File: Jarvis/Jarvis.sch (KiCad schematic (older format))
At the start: 139 parts, among them IC1 ADP1607, IC2 STM32F411CxUx, IC3 Si4460, IC4 MS5611-01BA03, IC5 MAX-8Q, IC6 MPU-9250, J1 PWR, J2 PYRO1, J3 ARM, J4 PYRO2, J5 PYRO3, J6 EXT, P1 SWD_TC, P2 SMA, Q1 NFET, Q2 NFET, Q3 NFET, Q4 NFET, Q5 PFET, Q6 PFET, Q7 PFET, U1 MICROSD, X1 434MHz ANT, X2 3mm LEDs, X3 ARM Switch, Y1 26MHz, Y2 30MHz

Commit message: Started PCB Layout
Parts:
- removed J2: PYRO1, agg:S02B-PASK-2, symbol CONN_01x02
- removed J4: PYRO2, agg:S02B-PASK-2, symbol CONN_01x02
- removed J5: PYRO3, agg:S02B-PASK-2, symbol CONN_01x02
- removed J6: EXT, symbol CONN_01x03
- removed Q4: NFET, symbol NFET
- removed Q6: PFET, symbol PFET
- removed R38, R39, R40: 10k, agg:0603-L, symbol R_Small
- added J2: PYRO, agg:S06B-PASK-2, symbol CONN_01x06
- added J4: EXT, agg:SIL-254P-04, symbol CONN_01x04
- added Q4: PFET, agg:SOT-23, symbol PFET
- added Q6: NFET, agg:SOT-23, symbol NFET
- added X4: Red LED, symbol PART
- D1, D2, D3: footprint (none) -> agg:0603-LED; Farnell (none) -> 1226372
- D4: footprint (none) -> agg:0603-LED; Farnell (none) -> 1226390
- IC5: footprint agg-unchecked:MAX-7Q -> Library:MAX-7Q
- IC6: footprint QFN-24-EP-MPU9250 -> agg:QFN-24-MPU9250
- J1: footprint (none) -> agg:S02B-PASK-2; Farnell 1702629 -> 1830747
- Q2, Q3: footprint (none) -> agg:SOT-23; Farnell (none) -> 1510761
- Q5, Q7: footprint (none) -> agg:SOT-23; Farnell (none) -> 1894738
- R10, R16: value R -> 100R; footprint agg:0603-L -> agg:0402-L; Farnell (none) -> 1358015
- R11, R12, R14: value R -> 10k; footprint agg:0603-L -> agg:0402-L; Farnell (none) -> 2072517
- R20, R22, R26: value 100R -> 10k; footprint agg:0603-L -> agg:0402-L; Farnell (none) -> 2072517
- R21: footprint agg:0603-L -> agg:0402-L; Farnell (none) -> 1358015
- R23, R24, R31, R36: footprint agg:0603-L -> agg:0402-L; Farnell (none) -> 2072517
- R25, R30, R35: value 10k -> 100R; footprint agg:0603-L -> agg:0402-L; Farnell (none) -> 1358015
- R27, R28: value 100R -> 1k; footprint agg:0603-L -> agg:0402-L; Farnell (none) -> 2072516
- R29, R37: value 10k -> 1k; footprint agg:0603-L -> agg:0402-L; Farnell (none) -> 2072516
- R32, R34: value 1R -> 10k; footprint agg:0603-L -> agg:0402-L; Farnell (none) -> 2072517
- R33: value 1R -> 1k; footprint agg:0603-L -> agg:0402-L; Farnell (none) -> 2072516
- R9: value R -> 1k; footprint agg:0603-L -> agg:0402-L; Farnell (none) -> 2072516
- X1, X3: footprint N/A -> (none)
- X2: value 3mm LEDs -> Green LED; Farnell (none) -> 1863180
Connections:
- net 3v3: now also R14.1, R24.1, R34.1
- net GND: now also R12.2, R31.2, J2.2, J2.4, J2.6, J4.3, J4.4, Q6.2 (S); no longer R24.2, R25.2
- net PYRO1: now also Q5.3 (D), R11.2, R14.2, J2.1; no longer R32.2, R33.2, R35.2
- net PYRO1_F: now also R10.1; no longer R20.1
- net PYRO1_S: now also R11.1; no longer R35.1
- net PYRO2: now also R22.2, R24.2, J2.3, Q4.3 (D); no longer R36.2
- net PYRO2_S: now also R22.1; no longer R36.1
- net PYRO3: now also Q7.3 (D), R32.2, R34.2, J2.5; no longer R37.2
- net PYRO3_F: now also R30.1; no longer R22.1
- net PYRO3_S: now also R32.1; no longer R37.1
- net PYRO_SO: now also R20.1, R26.1, R36.1, R37.1, Q4.2 (S); no longer R16.1, R29.1, R30.1, R31.1
- net STAT_EX_HBT: now also R33.1; no longer R14.1
- net STAT_HBT: now also R28.1; no longer R11.1
- net STAT_WRN: now also R29.1; no longer R12.1
- net VBATT: now also R27.1; no longer R10.1
- net at R10.2: now also Q2.1 (G), R12.1; no longer D2.2 (A)
- net at D3.2 (A): now also R28.2; no longer R11.2
- net at D4.2 (A): now also R29.2; no longer R12.2
- net at R16.2: now also Q5.1 (G), R20.2
- net at Q2.3 (D): now also R16.1; no longer R26.1
- net at Q3.1 (G), R21.2: now also R23.1; no longer R24.1
- net at Q3.3 (D): now also R25.1; no longer R27.1
- net at R30.2: now also R31.1, Q6.1 (G); no longer R27.2
- new net: J4.1, R33.2
- new net: J4.2, R37.2
- new net: Q4.1 (G), R25.2, R26.2
- new net: Q7.1 (G), R35.2, R36.2
- new net: Q6.3 (D), R35.1
- new net: D2.2 (A), R27.2
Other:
- note added: "External Parts:"
- note removed: "Contact RS regarding\nlead times"
- note removed: "J1 - FOOTPRINT REQUIRED"
- moved on the sheet: C17, C18, C19, C20, C21, C22, C23, C24, C25, C26, C27, C28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

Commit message: Schematic Complete
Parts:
- removed AE1: ANT, Library:SMA-142-0701-801, symbol ANT
- removed C25: 1uF, agg:0603-L, symbol C_Small
- removed J3: ARM, agg:S02B-PASK-2, symbol CONN_01x02
- removed J4: EXT, agg:SIL-254P-04, symbol CONN_01x04
- removed L4: 56nH, symbol L_Small
- removed L7: 18nH, Inductors_NEOSID:Neosid_Inductor_SM-NE29_SMD1008, symbol L_Small
- removed R33, R37: 1k, agg:0402-L, symbol R_Small
- removed X2: Green LED, symbol PART
- removed Y1: 26MHz, agg:XTAL-20x16, symbol XTAL
- added C33: 1uF, agg:0603-L, symbol C_Small
- added J3: ARM, agg:S03B-PASK-2, symbol CONN_01x03
- added L3, L6: 56nH, agg:0402-L, symbol L_Small
- added P1: SMA, Library:SMA-142-0701-801, symbol SMA
- added R25: 1k, agg:0402-L, symbol R_Small
- added X10, X8: Housing x1, symbol PART
- added X11: Housing x3, symbol PART
- added X12: M Crimps x6, symbol PART
- added X13: F Crimps x17, symbol PART
- added X14: Crimp Tool, symbol PART
- added X3: AA Battery, symbol PART
- added X4: AA Holder, symbol PART
- added X6: Wire, symbol PART
- added X7: Heat Shrink, symbol PART
- added X9: Housing x4, symbol PART
- added Y1: 26MHz, agg:XTAL-20x16, symbol SMD_XTAL
- C23: renamed from C19; footprint (none) -> agg:0402-L; Farnell (none) -> 1885321
- C24: renamed from C20; footprint (none) -> agg:0402-L; Farnell (none) -> 2310308
- C25: renamed from C21; footprint (none) -> agg:0402-L; Farnell (none) -> 1885342
- C26: renamed from C24; footprint (none) -> agg:0402-L; Farnell (none) -> 2310320
- C27: renamed from C26; footprint (none) -> agg:0402-L; Farnell (none) -> 1973025
- C28: footprint (none) -> agg:0402-L; Farnell (none) -> 2310320
- C32: renamed from C23; footprint (none) -> agg:0603-L; Farnell (none) -> 2346896
- C35: renamed from C29; footprint (none) -> agg:0402-L; Farnell (none) -> 2496792
- C36: renamed from C31; footprint (none) -> agg:0402-L; Farnell (none) -> 2496800
- L2: footprint Inductors_NEOSID:Neosid_Inductor_SM-NE29_SMD1008 -> agg:0402-L; Farnell (none) -> 1669639
- L4: renamed from L6; footprint Inductors_NEOSID:Neosid_Inductor_SM-NE29_SMD1008 -> agg:0402-L; Farnell (none) -> 1760988
- L5: value 56nH -> 18nH; footprint (none) -> agg:0402-L; Farnell (none) -> 1760988
- L7: renamed from L3; footprint Inductors_NEOSID:Neosid_Inductor_SM-NE29_SMD1008 -> agg:0603-L; Farnell (none) -> 2215631
- P2: Farnell (none) -> 1608592
- R32: renamed from R17; footprint agg:0603-L -> agg:0402-L; Farnell (none) -> 1469661
- Y2: Farnell (none) -> 2506973
- renumbered C30 to C1, C32 to C10, C33 to C11, C2 to C12, C5 to C13, C9 to C14, C34 to C15, C3 to C16, C6 to C17, C10 to C18, C14 to C19, C15 to C2, C7 to C20, C11 to C21, C12 to C22, C17 to C29, C16 to C3, C22 to C30, C13 to C31, C27 to C34, C18 to C37, C35 to C4, C36 to C5, C37 to C6, C1 to C7, C4 to C8, C8 to C9, IC5 to IC2, IC6 to IC3, IC2 to IC4, IC3 to IC5, IC4 to IC6, J2 to J1, J1 to J2, P1 to P3, Q5 to Q1, Q4 to Q2, Q7 to Q3, Q2 to Q4, Q3 to Q5, Q1 to Q7, R20 to R1, R30 to R10, R7 to R11, R23 to R13, R31 to R14, R14 to R15, R24 to R16, R34 to R17, R11 to R18, R22 to R19, R26 to R2, R32 to R20, R9 to R21, R27 to R22, R28 to R23, R29 to R24, R6 to R26, R1 to R27, R2 to R28, R3 to R29, R36 to R3, R4 to R30, R5 to R31, R19 to R33, R18 to R34, R13 to R35, R15 to R36, R16 to R4, R25 to R5, R35 to R6, R8 to R7, R10 to R8, R21 to R9, TP14 to TP1, TP3 to TP10, TP4 to TP11, TP5 to TP12, TP6 to TP13, TP7 to TP14, TP8 to TP15, TP9 to TP16, TP10 to TP17, TP11 to TP18, TP12 to TP19, TP15 to TP2, TP13 to TP20, TP16 to TP3, TP17 to TP4, TP18 to TP5, TP19 to TP6, TP20 to TP7, TP1 to TP8, TP2 to TP9, X4 to X2, X3 to X5
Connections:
- net STAT_EX_HBT is gone; now on net STAT_WRN: IC4.2 (PC13)
- net 3v3: now also C33.1
- net GND: now also C33.2, P1.2 (GND), P1.3 (GND), P1.4 (GND), P1.5 (GND), R25.2, Y1.2, Y1.4; no longer IC5.5 (NC)
- net PYRO_SO: now also J3.2
- net STAT_WRN: no longer IC4.4 (PC15)
- net VBATT: now also J3.1
- net at C21.2, IC4.5 (PH0): now also Y1.1
- net at IC2.11 (RF_IN): now also P1.1 (RF)
- net at C23.2, IC5.2 (RXp), L2.2: now also L3.1
- net at C22.2, R26.1: now also Y1.3
- net at C28.1, R32.1: now also L5.2
- net at C27.1, L4.2: now also L5.1
- net at C24.2, C26.1, L4.1: now also L3.2, L6.2; no longer L5.2
- net at C25.2: now also L6.1; no longer L5.1
- new net: J3.3, R25.1
- no-connect marks 15 -> 16
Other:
- note added: "Camera will have its\nown power supply ect."
- note added: "External HBT & Status\nindication will be done\nthrough sounder & radio"
- note added: "Notes:"
- note added: "Red 3mm LED wired in\nparallel with keyswitch\nto provide pyro status."
- note added: "TODO: Select Wire, Heatshrink & Crimps"
- note added: "X1"
- note added: "X1 434MHz Stubby Radio Antenna\nX2 Red Indicator LED for Pyro Arming\nX3 Energizer L91 Lithium Ultimate AA\nX4 AA Battery Holder\nX5 Key Switch for Arming Pyrotechnics\nX6 Wire\nX7 Heatshrink"
- note added: "X10"
- note added: "X11"
- note added: "X12"
- note added: "X13"
- note added: "X14"
- note added: "X2"
- note added: "X3\n"
- note added: "X4"
- note added: "X5"
- note added: "X6"
- note added: "X7"
- note added: "X8"
- note added: "X8 3 Pin Housing\nX9 2 Pin Housing\nX10 6 Pin Housing\nX11 2 Pin Recepticle\nX12 Male Crimps\nX13 Femal Crimps\nX14 Crimp Tool"
- note added: "X9"
- note removed: "COMPONENT SELECTION"
- note removed: "NB. Camera will have its\nown external 5v Supply."
- moved on the sheet: C21, C22, D1, D2, D3, D4, J2, R21, R22, R23, R24, X2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

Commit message: Added Testpoints
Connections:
- net GND: now also IC5.5 (NC)
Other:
- note added: "TODO:"
- note added: "TODO: Add Test Points & M2 Mounts"
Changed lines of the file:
@@
 Text Notes 6650 8250 0    60   Italic 0
 TODO: Select Wire, Heatshrink & Crimps
+Wire Wire Line
+	5900 7650 5950 7650
+Wire Wire Line
+	5950 7650 5950 7700
+$Comp
+L GND #PWR?
+U 1 1 56FD5801
+P 5950 7700
+F 0 "#PWR?" H 5950 7450 50  0001 C CNN
+F 1 "GND" H 5950 7550 50  0000 C CNN
+F 2 "" H 5950 7700 50  0000 C CNN
+F 3 "" H 5950 7700 50  0000 C CNN
+	1    5950 7700
+	1    0    0    -1
+$EndComp
+Text Notes 11850 10100 0    60   Italic 0
+TODO: Add Test Points & M2 Mounts
+Text Notes 11850 10100 0    60   Italic 12
+TODO:
+Text Notes 6650 8250 0    60   Italic 12
+TODO:
 $EndSCHEMATC

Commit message: Started PCB layout
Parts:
- added D10, D5, D6, D7, D8, D9: ESD_DIODE, agg:0402-L, symbol ESD_DIODE
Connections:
- net GND: now also D10.1, D5.1, D6.1, D7.1, D8.1, D9.1
- net PYRO1: now also D9.2
- net PYRO2: now also D8.2
- net PYRO3: now also D7.2
- net PYRO_SO: now also D10.2
- net VBATT: now also J3.3, D5.2, D6.2; no longer J3.1
- net at R25.1: now also J3.1; no longer J3.3
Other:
- moved on the sheet: J1, J2, J3, R25

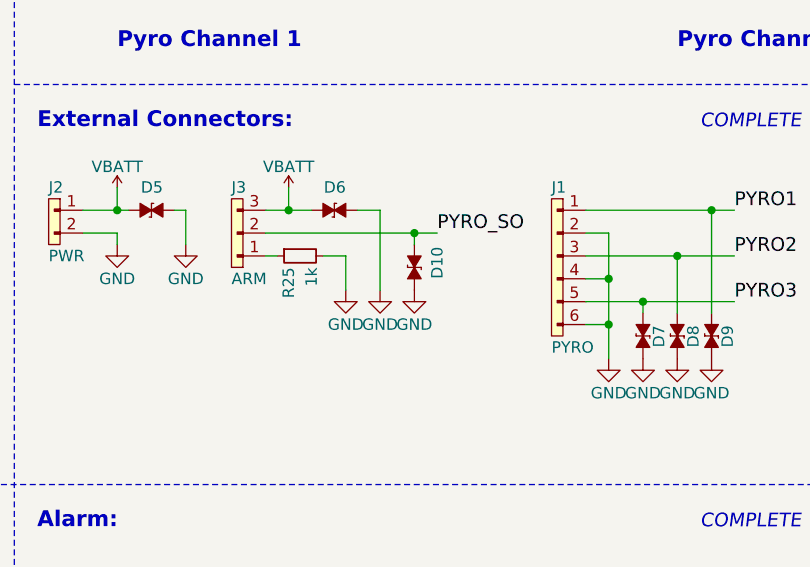
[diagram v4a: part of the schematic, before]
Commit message: Routed PSU
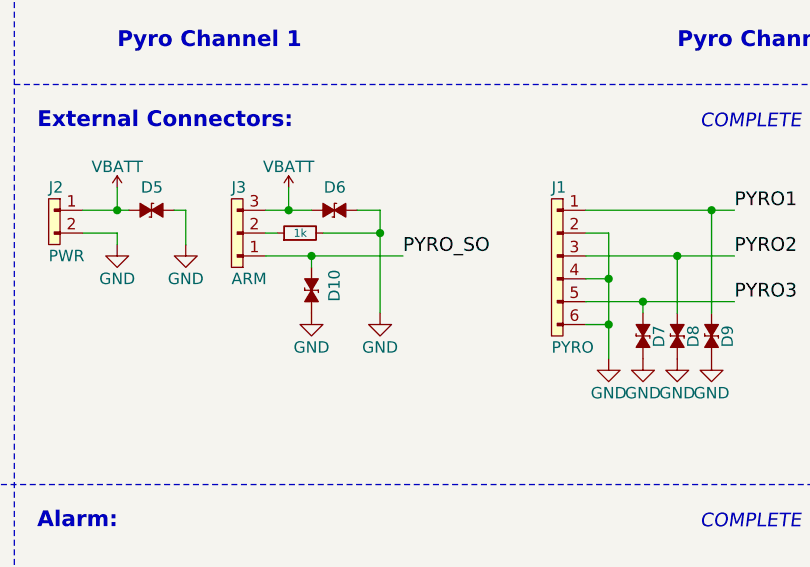
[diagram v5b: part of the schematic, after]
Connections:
- net PYRO_SO: now also J3.1; no longer J3.2
- net at R25.1: now also J3.2; no longer J3.1
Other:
- moved on the sheet: D10
